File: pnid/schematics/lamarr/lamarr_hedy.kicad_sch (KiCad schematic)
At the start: 98 parts

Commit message: Changed PniD
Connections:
- net at engine.~ (O): now also venturi1.~; no longer ox_venturi.~
- net at venturi1.~: now also fuel_main_valve.~, fuel_venturi_pressure.~; no longer engine.~ (O)
- net at dewar_needle_valve?.~: now also C2.~, C3.~; no longer C1.~
- net at Orifice2.~: now also fuel_pressurant_valve.~, pressurantPressureRegulator1.~
- new net: engine.~ (O), ox_venturi.~
- new net: OX.~, ox_main_valve.~, ox_quick_connect.~
- new net: DewarOverPressureValve?.~, LOX.~, dewar_pressurize_solenoid.~
- new net: C1.~, dewar_needle_valve?.~
- new net: Orifice1.~, ox_pressurant_valve.~, pressurantPressureRegulator2.~
- new net: FUEL.~, fuel_main_valve.~, ox_quick_connect1.~
- now unconnected: Orifice1.~
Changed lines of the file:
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@@
 	(wire
 		(pts
+			(xy 127 33.02) (xy 132.08 33.02)
+		)
+		(stroke
+			(width 0)
+			(type default)
+		)
+	)
+	(wire
+		(pts
 			(xy 78.486 114.3) (xy 78.486 118.11)
 		)
@@
 	(symbol
 		(lib_id "PnID-Lib:Sensor_Temperature")
-		(at 134.62 95.25 0)
+		(at 139.7 33.02 0)
 		(unit 1)
 		(exclude_from_sim no)
@@
 		(dnp no)
 		(property "Reference" "burst_disk_temperature"
-			(at 138.43 94.615 0)
+			(at 143.51 32.385 0)
 			(effects
 				(font
@@
 		)
 		(property "Value" "ox_temp_0:sensor"
-			(at 135.636 90.17 0)
+			(at 140.716 27.94 0)
 			(effects
 				(font
@@
 		)
 		(property "Footprint" ""
-			(at 134.62 95.25 0)
+			(at 139.7 33.02 0)
 			(effects
 				(font
@@
 		)
 		(property "Datasheet" ""
-			(at 134.62 95.25 0)
+			(at 139.7 33.02 0)
 			(effects
 				(font
@@
 		)
 		(property "Description" ""
-			(at 134.62 95.25 0)
+			(at 139.7 33.02 0)
 			(effects
 				(font
@@
 		)
 		(property "Unit" "˚C"
-			(at 134.62 95.25 0)
+			(at 139.7 33.02 0)
 			(effects
 				(font
@@
 		)
 		(property "Action_Reference" " "
-			(at 134.62 95.25 0)
+			(at 139.7 33.02 0)
 			(effects
 				(font

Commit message: dump uncommitted changes
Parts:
- removed fuel_pi_controller: fuel_pi_controller:Enabled, symbol PnID:Label
- removed ox_pi_controller: ox_pi_controller:Enabled, symbol PnID:Label
- removed pressure_control: pressurant_tanking_control:Enabled, symbol PnID:Label
- added dewar_pressure: dewar_pressure:sensor, symbol PnID-Lib:Sensor_Pressure
- added pneumatic_pressure: press_in:sensor, symbol PnID-Lib:Sensor_Pressure
- added ventilinsel_pressure: ventilinsel_pressure:sensor, symbol PnID-Lib:Sensor_Pressure
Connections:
- net at engine.~ (O): now also venturi1.~; no longer ox_venturi.~
- net at venturi1.~: now also fuel_main_valve.~, fuel_venturi_pressure.~; no longer engine.~ (O)
- net at dewar_needle_valve?.~: now also C2.~, C3.~; no longer C1.~
- net at Orifice2.~: now also fuel_pressurant_valve.~, pressurantPressureRegulator1.~
- new net: engine.~ (O), ox_venturi.~
- new net: OX.~, ox_main_valve.~, ox_quick_connect.~
- new net: DewarOverPressureValve?.~, LOX.~, dewar_pressurize_solenoid.~
- new net: C1.~, dewar_needle_valve?.~
- new net: Orifice1.~, ox_pressurant_valve.~, pressurantPressureRegulator2.~
- new net: FUEL.~, fuel_main_valve.~, ox_quick_connect1.~
- now unconnected: Orifice1.~
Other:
- note removed: "PI Controllers"

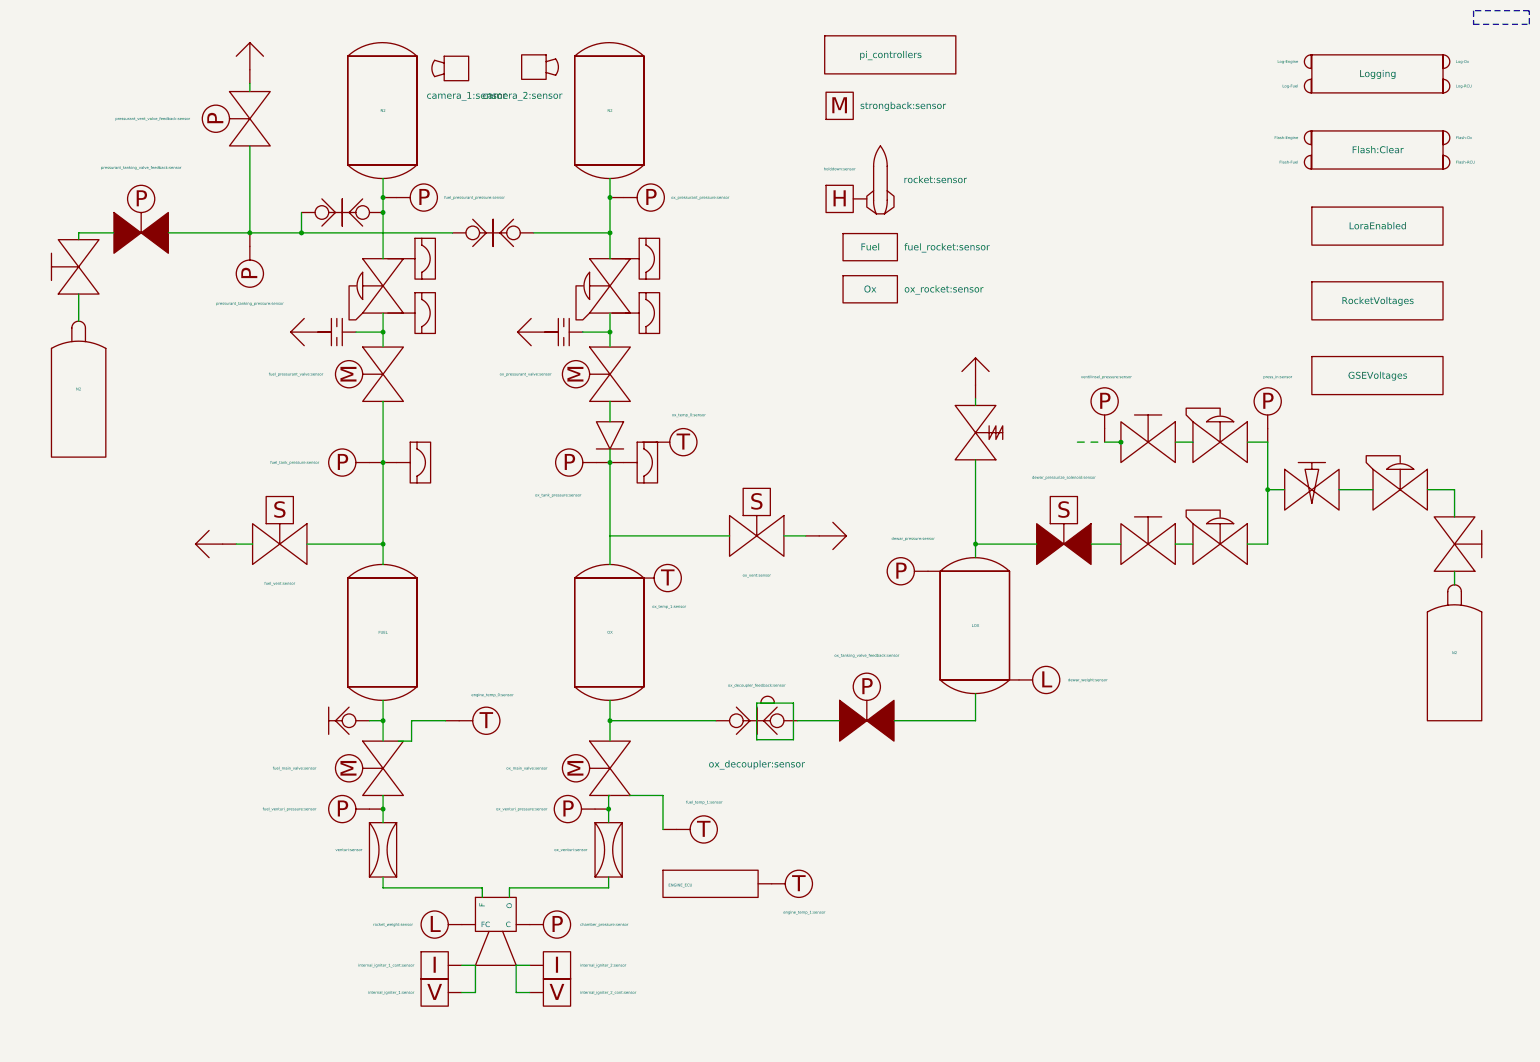
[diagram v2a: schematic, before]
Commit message: add safety light to pnid and llserver mapping
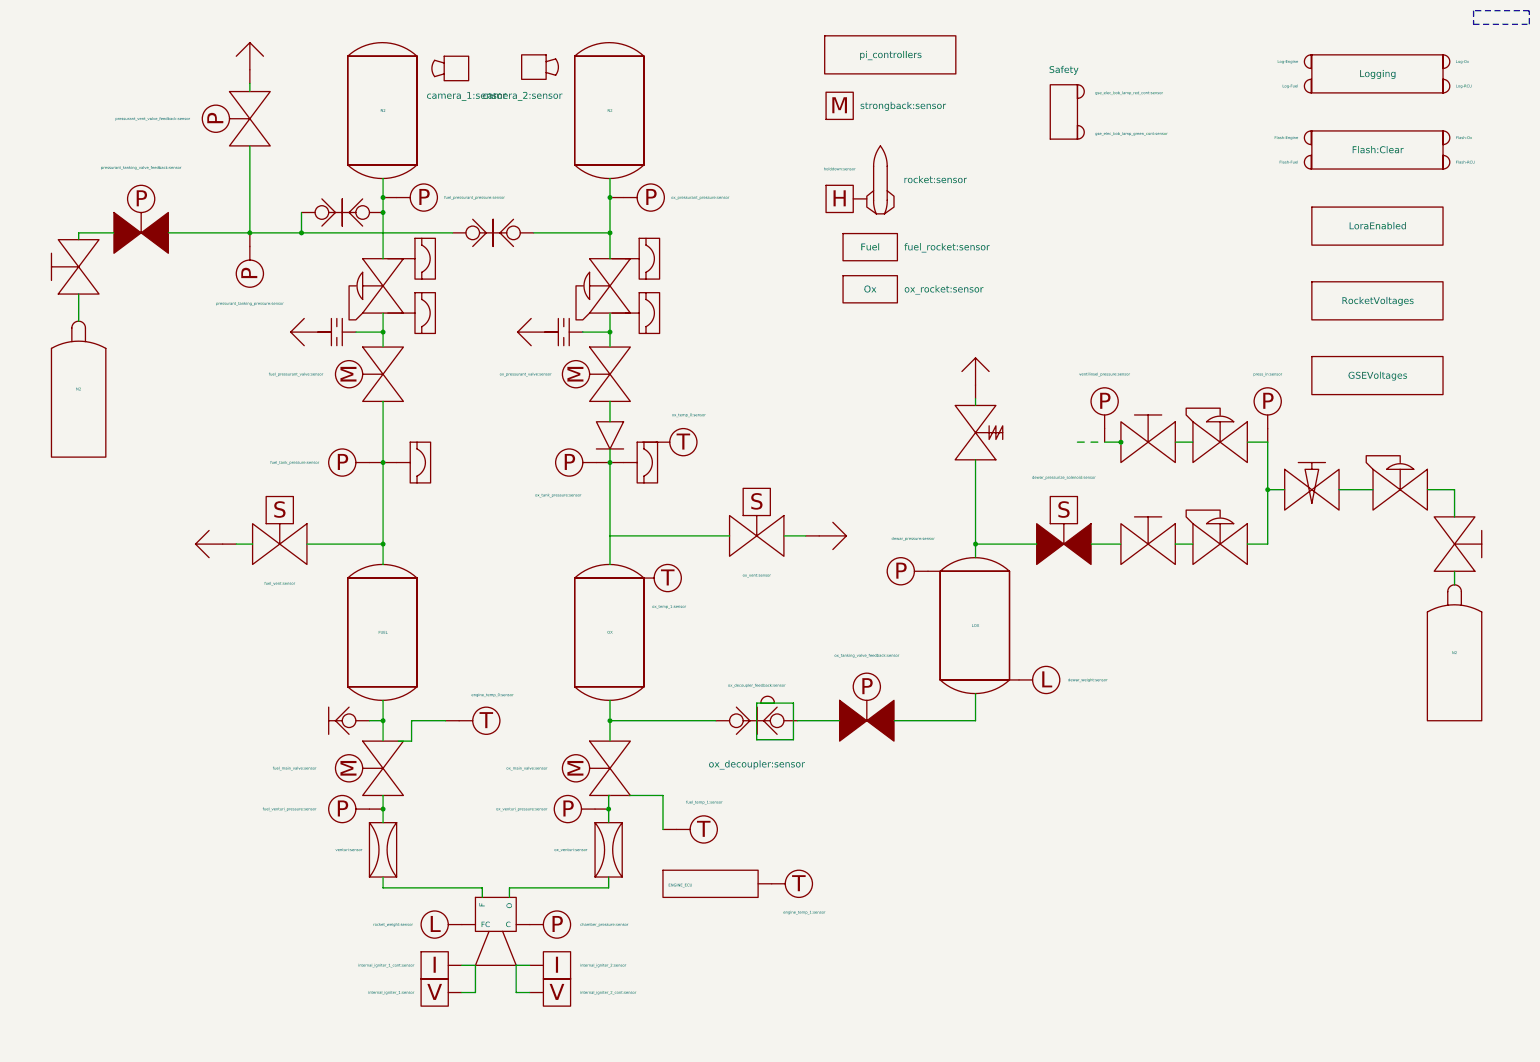
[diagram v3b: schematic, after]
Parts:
- added Green: gse_elec_bob_lamp_green_cont:sensor, symbol PnID-Lib:LED
- added Red: gse_elec_bob_lamp_red_cont:sensor, symbol PnID-Lib:LED
- added Safety: safety_light, symbol PnID-Lib:Flowchart_State
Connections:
- net at engine.~ (C): now also venturi1.~; no longer ox_venturi.~
- net at venturi1.~: now also fuel_main_valve.~, fuel_venturi_pressure.~; no longer engine.~ (O)
- net at dewar_needle_valve?.~: now also C2.~, C3.~; no longer C1.~
- net at Orifice2.~: now also fuel_pressurant_valve.~, pressurantPressureRegulator1.~
- new net: engine.~ (C), ox_venturi.~
- new net: OX.~, ox_main_valve.~, ox_quick_connect.~
- new net: DewarOverPressureValve?.~, LOX.~, dewar_pressurize_solenoid.~
- new net: C1.~, dewar_needle_valve?.~
- new net: Orifice1.~, ox_pressurant_valve.~, pressurantPressureRegulator2.~
- new net: FUEL.~, fuel_main_valve.~, ox_quick_connect1.~
- now unconnected: Orifice1.~
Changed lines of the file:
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@@
 (kicad_sch
-	(version 20231120)
+	(version 20250114)
 	(generator "eeschema")
-	(generator_version "8.0")
+	(generator_version "9.0")
 	(paper "A4")
 	(junction
@@
 		)
 		(property "Value" "press_in:sensor"
-			(at 248.412 83.058 0)
+			(at 243.84 82.55 0)
 			(effects
 				(font
 					(size 0.508 0.508)
 				)
-				(justify left)
 			)
 		)
@@
 	(symbol
 		(lib_id "PnID-Lib:LED")
+		(at 208.788 37.338 270)
+		(unit 1)
+		(exclude_from_sim no)
+		(in_bom yes)
+		(on_board yes)
+		(dnp no)
+		(property "Reference" "Green"
+			(at 209.55 39.624 0)
+			(effects
+				(font
+					(size 0.508 0.508)
+				)
+				(justify left)
+				(hide yes)
+			)
+		)
+		(property "Value" "gse_elec_bob_lamp_green_cont:sensor"
+			(at 211.582 37.592 90)
+			(effects
+				(font
+					(size 0.508 0.508)
+				)
+				(justify left)
+			)
+		)
+		(property "Footprint" ""
+			(at 208.788 37.338 0)
+			(effects
+				(font
+					(size 0.508 0.508)
+				)
+				(hide yes)
+			)
+		)
+		(property "Datasheet" ""
+			(at 208.788 37.338 0)
+			(effects
+				(font
+					(size 0.508 0.508)
+				)
+				(hide yes)
+			)
+		)
+		(property "Description" ""
+			(at 208.788 37.338 0)
+			(effects
+				(font
+					(size 1.27 1.27)
+				)
+				(hide yes)
+			)
+		)
+		(property "Action_Reference" "gui:safety_light"
+			(at 208.788 37.338 0)
+			(effects
+				(font
+					(size 1.27 1.27)
+				)
+				(hide yes)
+			)
+		)
+		(instances
+			(project "lamarr_hedy"
+				(path "/604fc9f3-63a6-4133-afd1-4a5c2507dc1d"
+					(reference "Green")
+					(unit 1)
+				)
+			)
+		)
+	)
+	(symbol
+		(lib_id "PnID-Lib:LED")
 		(at 251.46 38.354 90)
 		(unit 1)
@@
 	)
 	(symbol
+		(lib_id "PnID-Lib:Flowchart_State")
+		(at 205.74 33.528 90)
+		(unit 1)
+		(exclude_from_sim no)
+		(in_bom yes)
+		(on_board yes)
+		(dnp no)
+		(property "Reference" "Safety"
+			(at 205.74 25.654 90)
+			(effects
+				(font
+					(size 1.27 1.27)
+				)
+			)
+		)
+		(property "Value" "safety_light"
+			(at 205.7399 27.178 0)
+			(effects
+				(font
+					(size 1.27 1.27)
+				)
+				(justify left)
+				(hide yes)
+			)
+		)
+		(property "Footprint" ""
+			(at 205.74 33.528 0)
+			(effects
+				(font
+					(size 1.27 1.27)
+				)
+				(hide yes)
+			)
+		)
+		(property "Datasheet" ""
+			(at 205.74 33.528 0)
+			(effects
+				(font
+					(size 1.27 1.27)
+				)
+				(hide yes)
+			)
+		)
+		(property "Description" ""
+			(at 205.74 33.528 0)
+			(effects
+				(font
+					(size 1.27 1.27)
+				)
+				(hide yes)
+			)
+		)
+		(property "Action_Reference" "gui:safety_light"
+			(at 205.74 33.528 90)
+			(effects
+				(font
+					(size 1.27 1.27)
+				)
+				(hide yes)
+			)
+		)
+		(instances
+			(project "lamarr_hedy"
+				(path "/604fc9f3-63a6-4133-afd1-4a5c2507dc1d"
+					(reference "Safety")
+					(unit 1)
+				)
+			)
+		)
+	)
+	(symbol
 		(lib_id "PnID-Lib:QuickConnect_Half")
 		(at 68.326 147.32 180)
@@
 		)
 		(property "Value" "ventilinsel_pressure:sensor"
-			(at 218.44 83.058 0)
+			(at 213.36 82.55 0)
 			(effects
 				(font
 					(size 0.508 0.508)
 				)
-				(justify left)
 			)
 		)
@@
 	)
 	(symbol
+		(lib_id "PnID-Lib:LED")
+		(at 208.788 29.718 270)
+		(unit 1)
+		(exclude_from_sim no)
+		(in_bom yes)
+		(on_board yes)
+		(dnp no)
+		(property "Reference" "Red"
+			(at 209.55 32.004 0)
+			(effects
+				(font
+					(size 0.508 0.508)
+				)
+				(justify left)
+				(hide yes)
+			)
+		)
+		(property "Value" "gse_elec_bob_lamp_red_cont:sensor"
+			(at 211.582 29.972 90)
+			(effects
+				(font
+					(size 0.508 0.508)
+				)
+				(justify left)
+			)
+		)
+		(property "Footprint" ""
+			(at 208.788 29.718 0)
+			(effects
+				(font
+					(size 0.508 0.508)
+				)
+				(hide yes)
+			)
+		)
+		(property "Datasheet" ""
+			(at 208.788 29.718 0)
+			(effects
+				(font
+					(size 0.508 0.508)
+				)
+				(hide yes)
+			)
+		)
+		(property "Description" ""
+			(at 208.788 29.718 0)
+			(effects
+				(font
+					(size 1.27 1.27)
+				)
+				(hide yes)
+			)
+		)
+		(property "Action_Reference" "gui:safety_light"
+			(at 208.788 29.718 0)
+			(effects
+				(font
+					(size 1.27 1.27)
+				)
+				(hide yes)
+			)
+		)
+		(instances
+			(project "lamarr_hedy"
+				(path "/604fc9f3-63a6-4133-afd1-4a5c2507dc1d"
+					(reference "Red")
+					(unit 1)
+				)
+			)
+		)
+	)
+	(symbol
 		(lib_id "PnID-Lib:Tank_Slim")
 		(at 78.486 33.274 0)
@@
 		)
 	)
+	(embedded_fonts no)
 )

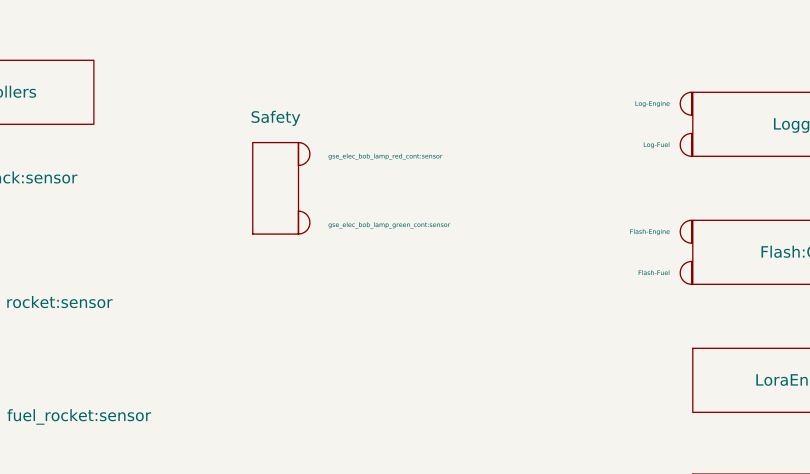
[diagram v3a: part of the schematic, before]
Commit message: fix safety light implementation
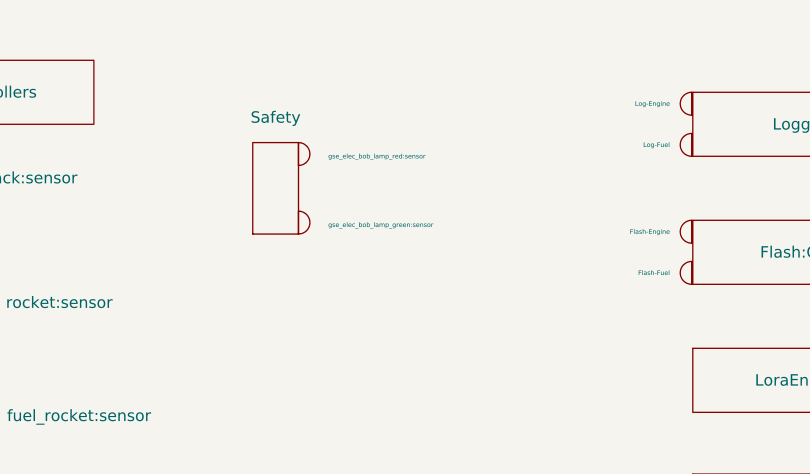
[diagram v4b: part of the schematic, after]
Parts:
- Green: value gse_elec_bob_lamp_green_cont:sensor -> gse_elec_bob_lamp_green:sensor
- Red: value gse_elec_bob_lamp_red_cont:sensor -> gse_elec_bob_lamp_red:sensor
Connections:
- net at engine.~ (C): now also venturi1.~; no longer ox_venturi.~
- net at venturi1.~: now also fuel_main_valve.~, fuel_venturi_pressure.~; no longer engine.~ (C)
- net at dewar_needle_valve?.~: now also C2.~, C3.~; no longer C1.~
- net at Orifice2.~: now also fuel_pressurant_valve.~, pressurantPressureRegulator1.~
- new net: engine.~ (C), ox_venturi.~
- new net: OX.~, ox_main_valve.~, ox_quick_connect.~
- new net: DewarOverPressureValve?.~, LOX.~, dewar_pressurize_solenoid.~
- new net: C1.~, dewar_needle_valve?.~
- new net: Orifice1.~, ox_pressurant_valve.~, pressurantPressureRegulator2.~
- new net: FUEL.~, fuel_main_valve.~, ox_quick_connect1.~
- now unconnected: Orifice1.~
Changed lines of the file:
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@@
 			)
 		)
-		(property "Value" "gse_elec_bob_lamp_green_cont:sensor"
+		(property "Value" "gse_elec_bob_lamp_green:sensor"
 			(at 211.582 37.592 90)
 			(effects
@@
 			)
 		)
-		(property "Value" "gse_elec_bob_lamp_red_cont:sensor"
+		(property "Value" "gse_elec_bob_lamp_red:sensor"
 			(at 211.582 29.972 90)
 			(effects
